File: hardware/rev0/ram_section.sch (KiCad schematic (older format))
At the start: 2 parts, among them IC1 ECP5-BGA256, U10 S27KS0641

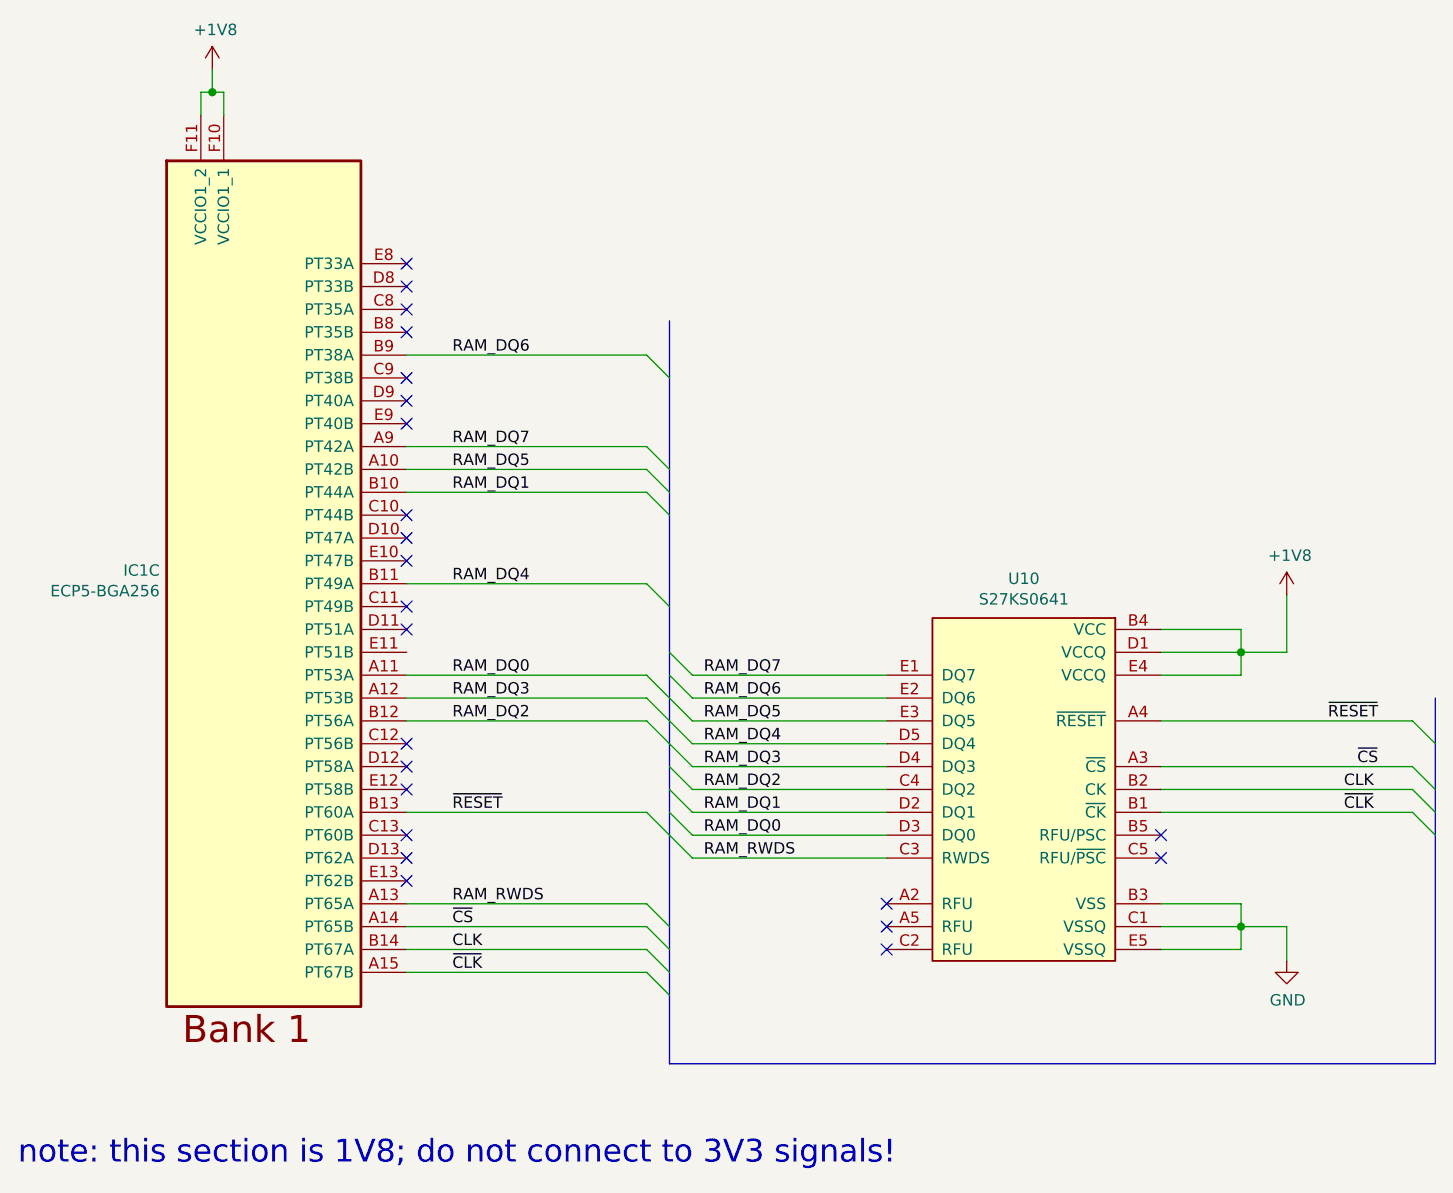
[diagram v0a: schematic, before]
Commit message: Switch to 3V3 for RAM, remove 1V8 rail
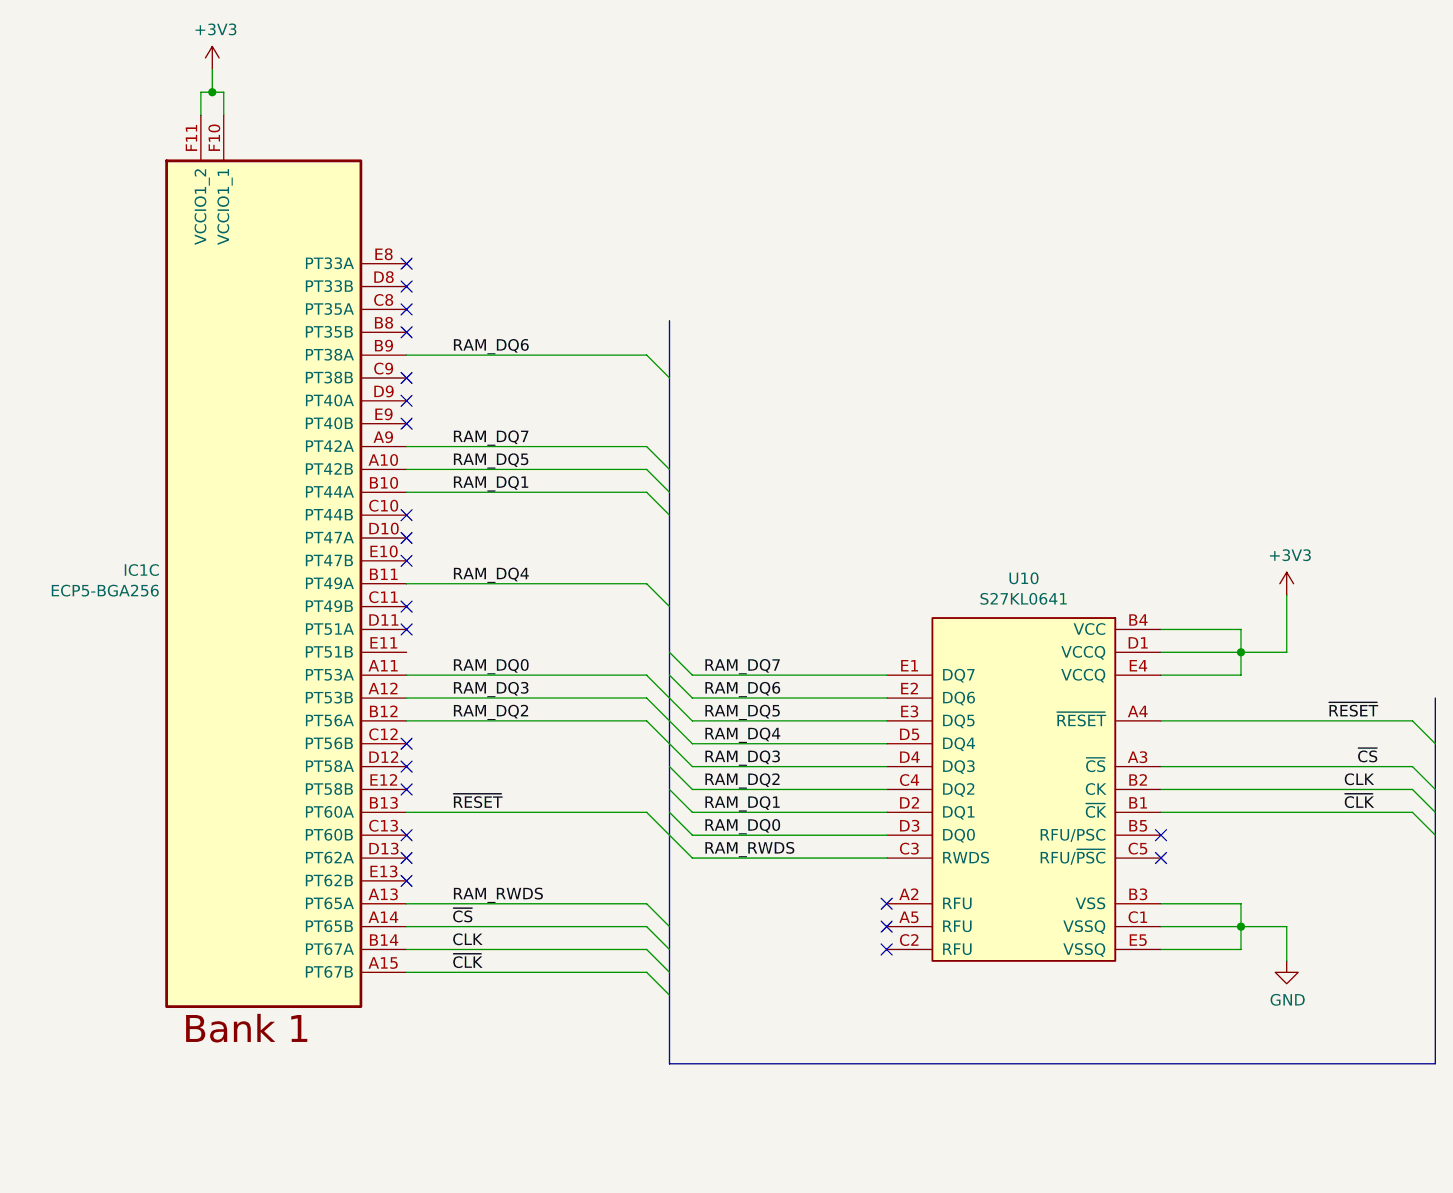
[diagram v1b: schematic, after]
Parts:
- U10: value S27KS0641 -> S27KL0641
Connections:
- net +1V8 renamed +3V3
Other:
- note removed: "note: this section is 1V8; do not connect to 3V3 signals!"
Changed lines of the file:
@@
 	1850 1800 1900 1800
-$Comp
-L power:+1V8 #PWR081
-U 1 1 5DE84804
-P 1850 1700
-F 0 "#PWR081" H 1850 1550 50  0001 C CNN
-F 1 "+1V8" H 1864 1873 50  0000 C CNN
-F 2 "" H 1850 1700 50  0001 C CNN
-F 3 "" H 1850 1700 50  0001 C CNN
-	1    1850 1700
-	1    0    0    -1
-$EndComp
 $Comp
 L fpgas_and_processors:ECP5-BGA256 IC1
@@
 P 5400 4850
 F 0 "U10" H 5400 5772 50  0000 C CNN
-F 1 "S27KS0641" H 5400 5682 50  0000 C CNN
+F 1 "S27KL0641" H 5400 5682 50  0000 C CNN
 F 2 "amalthea:BGA-24_5x5_6.0x8.0mm" H 6000 3950 50  0001 C CNN
 F 3 "" H 5400 3950 50  0001 C CNN
@@
 	-1   0    0    -1
 $EndComp
-Text Notes 1000 6500 0    100  ~ 0
-note: this section is 1V8; do not connect to 3V3 signals!
 Wire Wire Line
 	6000 4150 6350 4150
@@
 Wire Wire Line
 	6550 4250 6550 4000
-$Comp
-L power:+1V8 #PWR084
-U 1 1 5DEA6771
-P 6550 4000
-F 0 "#PWR084" H 6550 3850 50  0001 C CNN
-F 1 "+1V8" H 6564 4173 50  0000 C CNN
-F 2 "" H 6550 4000 50  0001 C CNN
-F 3 "" H 6550 4000 50  0001 C CNN
-	1    6550 4000
-	1    0    0    -1
-$EndComp
 Wire Wire Line
 	6000 5350 6350 5350
@@
 Wire Bus Line
 	3850 2800 3850 6050
+$Comp
+L power:+3V3 #PWR0106
+U 1 1 5EA239A6
+P 1850 1700
+F 0 "#PWR0106" H 1850 1550 50  0001 C CNN
+F 1 "+3V3" H 1865 1873 50  0000 C CNN
+F 2 "" H 1850 1700 50  0001 C CNN
+F 3 "" H 1850 1700 50  0001 C CNN
+	1    1850 1700
+	1    0    0    -1
+$EndComp
+$Comp
+L power:+3V3 #PWR0107
+U 1 1 5EA2585C
+P 6550 4000
+F 0 "#PWR0107" H 6550 3850 50  0001 C CNN
+F 1 "+3V3" H 6565 4173 50  0000 C CNN
+F 2 "" H 6550 4000 50  0001 C CNN
+F 3 "" H 6550 4000 50  0001 C CNN
+	1    6550 4000
+	1    0    0    -1
+$EndComp
 $EndSCHEMATC

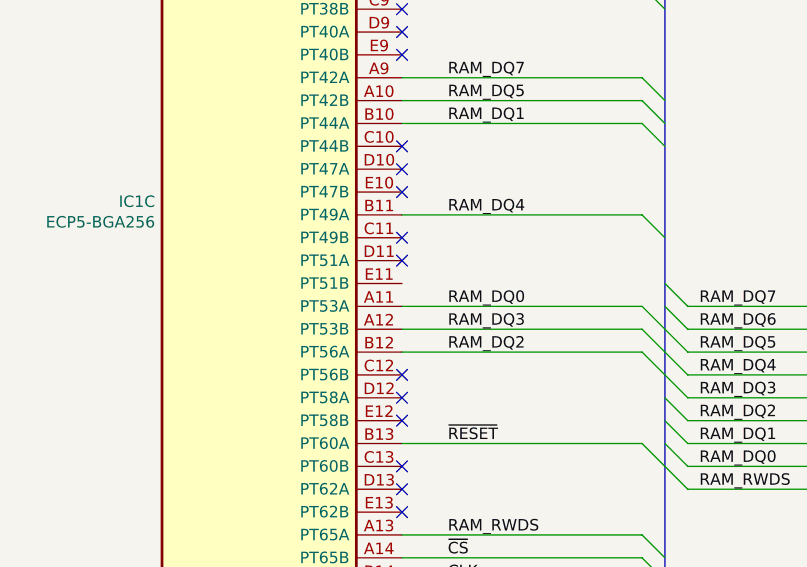
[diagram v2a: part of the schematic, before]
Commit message: Route/NC remaining target signals, ERC & schematic cleanup
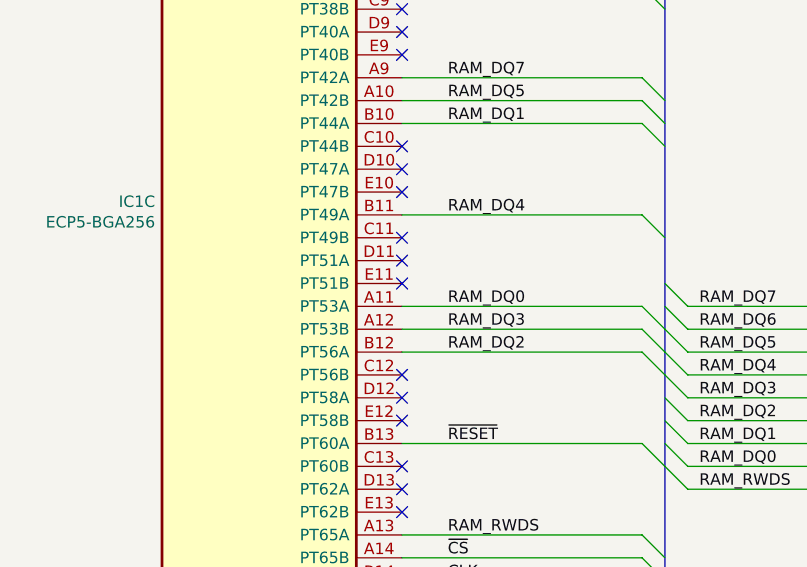
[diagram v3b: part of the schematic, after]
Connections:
- no-connect marks 23 -> 24
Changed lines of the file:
@@
 	1    0    0    -1
 $EndComp
+NoConn ~ 2700 4250
 Wire Bus Line
 	7200 4450 7200 6050

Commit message: Pick part numbers for BOM
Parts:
- U10: Manufacturer_Part_Number (none) -> S27KL0641
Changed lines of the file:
@@
 F 3 "" H 5400 3950 50  0001 C CNN
 F 4 "ANY" H 5400 4850 50  0001 C CNN "Source"
+F 5 "S27KL0641" H 5400 4850 50  0001 C CNN "Manufacturer_Part_Number"
 	1    5400 4850
 	-1   0    0    -1
